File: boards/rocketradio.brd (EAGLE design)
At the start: 229.5 x 167.6 mm, 6 parts, among them X1 BU-SMA-H

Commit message: moving to new repo
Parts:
- added U$2: ATTINY85SOCKET, evan:SOCKET-08
- added U$3, U$4, U$5, U$6, U$7, U$8, U$9: 1N4148W, evan:SOD123
- U$1: value (none) -> DRA818V
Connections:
- new net N$10: U$1.3
- new net N$11: U$1.16, U$6.A
- new net N$12: U$8.C, U$9.A
- new net N$13: U$7.C, U$8.A
- new net N$14: U$2.5, U$7.A
- new net N$15: U$6.C
- new net N$16: U$3.A
- new net N$6: U$1.17, U$4.C
- new net N$7: U$4.A, U$5.C
- new net N$8: U$3.C, U$5.A
- new net N$9: U$1.18
- net +3V3: now also R2.1
- net GND: no longer R2.1
- net N$4: now also U$9.C
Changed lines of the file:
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@@
 <layer number="101" name="top_pads" color="7" fill="4" visible="no" active="yes"/>
 <layer number="102" name="bot_pads" color="7" fill="5" visible="no" active="yes"/>
+<layer number="103" name="tMap" color="7" fill="1" visible="yes" active="yes"/>
 <layer number="104" name="S_DOKU" color="7" fill="1" visible="no" active="yes"/>
+<layer number="105" name="tPlate" color="7" fill="1" visible="yes" active="yes"/>
+<layer number="106" name="bPlate" color="7" fill="1" visible="yes" active="yes"/>
+<layer number="107" name="Crop" color="7" fill="1" visible="yes" active="yes"/>
+<layer number="108" name="tplace-old" color="10" fill="1" visible="yes" active="yes"/>
+<layer number="109" name="ref-old" color="11" fill="1" visible="yes" active="yes"/>
 <layer number="116" name="Patch_BOT" color="9" fill="4" visible="yes" active="yes"/>
 <layer number="121" name="_tsilk" color="7" fill="1" visible="yes" active="yes"/>
 <layer number="122" name="_bsilk" color="7" fill="1" visible="yes" active="yes"/>
+<layer number="125" name="_tNames" color="7" fill="1" visible="yes" active="yes"/>
+<layer number="144" name="Drill_legend" color="7" fill="1" visible="yes" active="yes"/>
 <layer number="151" name="HeatSink" color="7" fill="1" visible="yes" active="yes"/>
 <layer number="199" name="Contour" color="7" fill="1" visible="no" active="yes"/>
@@
 <layer number="207" name="207bmp" color="8" fill="10" visible="yes" active="yes"/>
 <layer number="208" name="208bmp" color="9" fill="10" visible="yes" active="yes"/>
+<layer number="209" name="209bmp" color="7" fill="1" visible="yes" active="yes"/>
+<layer number="210" name="210bmp" color="7" fill="1" visible="yes" active="yes"/>
+<layer number="211" name="211bmp" color="7" fill="1" visible="yes" active="yes"/>
+<layer number="212" name="212bmp" color="7" fill="1" visible="yes" active="yes"/>
+<layer number="213" name="213bmp" color="7" fill="1" visible="yes" active="yes"/>
+<layer number="214" name="214bmp" color="7" fill="1" visible="yes" active="yes"/>
+<layer number="215" name="215bmp" color="7" fill="1" visible="yes" active="yes"/>
+<layer number="216" name="216bmp" color="7" fill="1" visible="yes" active="yes"/>
+<layer number="217" name="217bmp" color="18" fill="1" visible="no" active="no"/>
+<layer number="218" name="218bmp" color="19" fill="1" visible="no" active="no"/>
+<layer number="219" name="219bmp" color="20" fill="1" visible="no" active="no"/>
+<layer number="220" name="220bmp" color="21" fill="1" visible="no" active="no"/>
+<layer number="221" name="221bmp" color="22" fill="1" visible="no" active="no"/>
+<layer number="222" name="222bmp" color="23" fill="1" visible="no" active="no"/>
+<layer number="223" name="223bmp" color="24" fill="1" visible="no" active="no"/>
+<layer number="224" name="224bmp" color="25" fill="1" visible="no" active="no"/>
 <layer number="250" name="Descript" color="3" fill="1" visible="no" active="no"/>
 <layer number="251" name="SMDround" color="12" fill="11" visible="no" active="no"/>
@@
 </autorouter>
 <elements>
-<element name="U$1" library="dorji" package="DORJI" value="" x="1.27" y="-24.13"/>
+<element name="U$1" library="dorji" package="DORJI" value="DRA818V" x="1.27" y="-24.13"/>
 <element name="X1" library="con-coax" package="BU-SMA-H" value="BU-SMA-H" x="5.08" y="-35.56">
 <attribute name="OC_NEWARK" value="unknown" x="5.08" y="-35.56" size="1.778" layer="27" display="off"/>
@@
 <element name="R3" library="rcl" package="R0603" value="10K" x="2.54" y="-52.07"/>
 <element name="R4" library="rcl" package="R0603" value="10K" x="2.54" y="-55.88"/>
+<element name="U$2" library="evan" package="SOCKET-08" value="ATTINY85SOCKET" x="7.62" y="-64.77"/>
+<element name="U$3" library="evan" package="SOD123" value="1N4148W" x="3.81" y="-73.66"/>
+<element name="U$4" library="evan" package="SOD123" value="1N4148W" x="3.81" y="-80.01"/>
+<element name="U$5" library="evan" package="SOD123" value="1N4148W" x="3.81" y="-86.36"/>
+<element name="U$6" library="evan" package="SOD123" value="1N4148W" x="3.81" y="-92.71"/>
+<element name="U$7" library="evan" package="SOD123" value="1N4148W" x="3.81" y="-99.06"/>
+<element name="U$8" library="evan" package="SOD123" value="1N4148W" x="3.81" y="-105.41"/>
+<element name="U$9" library="evan" package="SOD123" value="1N4148W" x="3.81" y="-111.76"/>
 </elements>
 <signals>
@@
 <contactref element="R3" pad="1"/>
 <contactref element="R1" pad="1"/>
-<contactref element="R2" pad="1"/>
 <contactref element="R4" pad="1"/>
 <wire x1="1.69" y1="-52.07" x2="1.69" y2="-55.88" width="0" layer="19" extent="1-1"/>
-<wire x1="1.69" y1="-48.26" x2="1.69" y2="-52.07" width="0" layer="19" extent="1-1"/>
-<wire x1="1.69" y1="-44.45" x2="1.69" y2="-48.26" width="0" layer="19" extent="1-1"/>
+<wire x1="1.69" y1="-44.45" x2="1.69" y2="-52.07" width="0" layer="19" extent="1-1"/>
 <wire x1="2.5301" y1="-38.1099" x2="1.69" y2="-44.45" width="0" layer="19" extent="1-1"/>
 <wire x1="7.6299" y1="-38.1099" x2="2.5301" y2="-38.1099" width="0" layer="19" extent="1-1"/>
@@
 <signal name="+3V3">
 <contactref element="U$1" pad="8"/>
+<contactref element="R2" pad="1"/>
+<wire x1="38.27" y1="-7.73" x2="1.69" y2="-48.26" width="0" layer="19" extent="1-1"/>
 </signal>
 <signal name="N$1">
@@
 <contactref element="R3" pad="2"/>
 <contactref element="U$1" pad="5"/>
+<contactref element="U$9" pad="C"/>
+<wire x1="3.39" y1="-52.07" x2="1.91" y2="-111.76" width="0" layer="19" extent="1-1"/>
 <wire x1="23.47" y1="-3.63" x2="3.39" y2="-52.07" width="0" layer="19" extent="1-1"/>
 </signal>
@@
 <wire x1="5.47" y1="-3.63" x2="3.39" y2="-55.88" width="0" layer="19" extent="1-1"/>
 </signal>
+<signal name="N$6">
+<contactref element="U$1" pad="17"/>
+<contactref element="U$4" pad="C"/>
+<wire x1="10.17" y1="-25.53" x2="1.91" y2="-80.01" width="0" layer="19" extent="1-1"/>
+</signal>
+<signal name="N$7">
+<contactref element="U$4" pad="A"/>
+<contactref element="U$5" pad="C"/>
+<wire x1="5.71" y1="-80.01" x2="1.91" y2="-86.36" width="0" layer="19" extent="1-1"/>
+</signal>
+<signal name="N$8">
+<contactref element="U$5" pad="A"/>
+<contactref element="U$3" pad="C"/>
+<wire x1="1.91" y1="-73.66" x2="5.71" y2="-86.36" width="0" layer="19" extent="1-1"/>
+</signal>
+<signal name="N$11">
+<contactref element="U$6" pad="A"/>
+<contactref element="U$1" pad="16"/>
+<wire x1="14.57" y1="-25.53" x2="5.71" y2="-92.71" width="0" layer="19" extent="1-1"/>
+</signal>
+<signal name="N$12">
+<contactref element="U$9" pad="A"/>
+<contactref element="U$8" pad="C"/>
+<wire x1="1.91" y1="-105.41" x2="5.71" y2="-111.76" width="0" layer="19" extent="1-1"/>
+</signal>
+<signal name="N$13">
+<contactref element="U$8" pad="A"/>
+<contactref element="U$7" pad="C"/>
+<wire x1="1.91" y1="-99.06" x2="5.71" y2="-105.41" width="0" layer="19" extent="1-1"/>
+</signal>
+<signal name="N$9">
+<contactref element="U$1" pad="18"/>
+</signal>
+<signal name="N$10">
+<contactref element="U$1" pad="3"/>
+</signal>
+<signal name="N$14">
+<contactref element="U$7" pad="A"/>
+<contactref element="U$2" pad="5"/>
+<wire x1="11.43" y1="-60.96" x2="5.71" y2="-99.06" width="0" layer="19" extent="1-1"/>
+</signal>
+<signal name="N$15">
+<contactref element="U$6" pad="C"/>
+</signal>
+<signal name="N$16">
+<contactref element="U$3" pad="A"/>
+</signal>
 </signals>

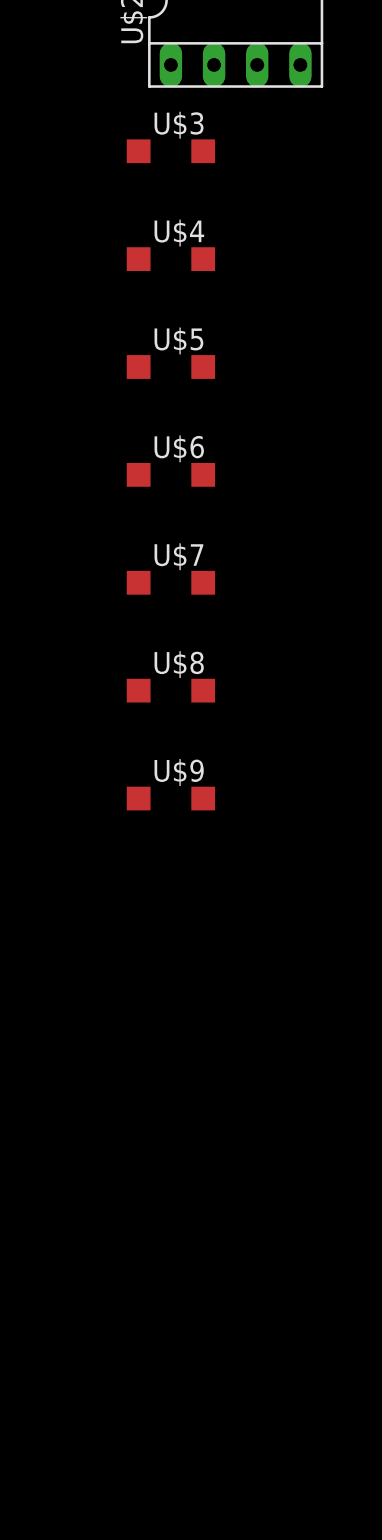
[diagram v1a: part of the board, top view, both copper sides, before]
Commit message: update board with correct modem pinout
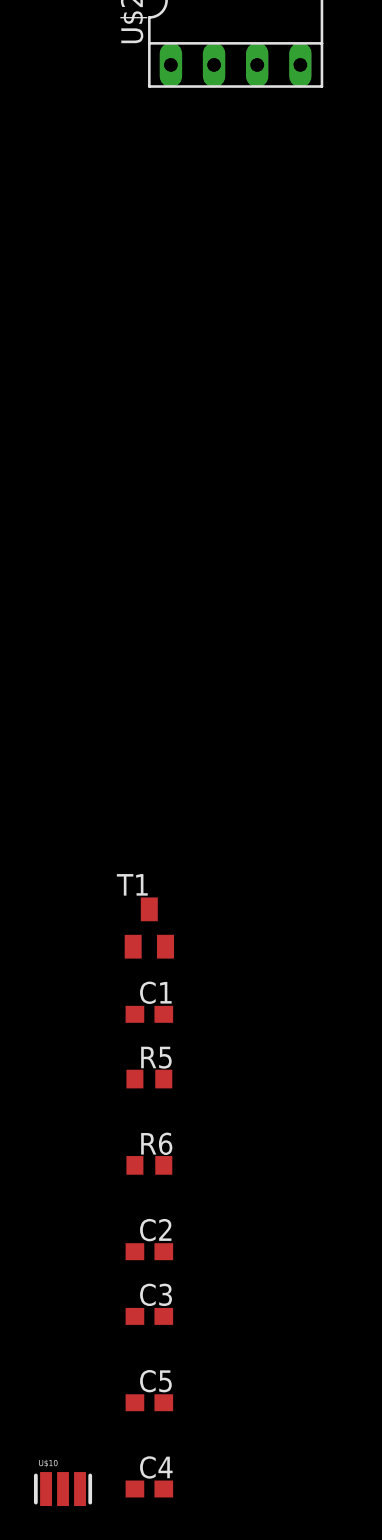
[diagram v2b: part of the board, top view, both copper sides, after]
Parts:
- removed U$3, U$4, U$5, U$6, U$7, U$8, U$9: 1N4148W, evan:SOD123
- added C1: (no value), rcl:C0603
- added C2, C4: 1uF, rcl:C0603
- added C3, C5: 0.1uF, rcl:C0603
- added R5: 30K, rcl:R0603
- added R6: 10K, rcl:R0603
- added T1: (no value), transistor:SOT23-BEC
- added U$10: CSTCE16M0V53-R0, evan:MYSMD2_RESONATOR
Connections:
- removed net N$10: U$1.3
- removed net N$11: U$1.16, U$6.A
- removed net N$12: U$8.C, U$9.A
- removed net N$13: U$7.C, U$8.A
- removed net N$14: U$2.5, U$7.A
- removed net N$4: R3.2, U$1.5, U$9.C
- removed net N$6: U$1.17, U$4.C
- removed net N$7: U$4.A, U$5.C
- removed net N$8: U$3.C, U$5.A
- new net MOD_IN: U$1.3, U$2.5
- new net MOD_OUT: U$2.6
- new net N$17: U$10.3, U$2.2
- new net N$18: U$10.1, U$2.3
- new net N$20: C1.1, R5.2, R6.1, T1.B
- new net SLAVE_SELECT: R3.2, U$1.5, U$2.1
- new net UART: U$2.7
- net +3V3: now also C2.1, C3.1, C4.1, C5.1, U$2.8
- net GND: now also C2.2, C3.2, C4.2, C5.2, U$10.2
- net N$15: now also U$1.16; no longer U$6.C
- net N$16: now also U$1.17; no longer U$3.A
- net N$9: now also C1.2
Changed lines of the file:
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@@
 <element name="R4" library="rcl" package="R0603" value="10K" x="2.54" y="-55.88"/>
 <element name="U$2" library="evan" package="SOCKET-08" value="ATTINY85SOCKET" x="7.62" y="-64.77"/>
-<element name="U$3" library="evan" package="SOD123" value="1N4148W" x="3.81" y="-73.66"/>
-<element name="U$4" library="evan" package="SOD123" value="1N4148W" x="3.81" y="-80.01"/>
-<element name="U$5" library="evan" package="SOD123" value="1N4148W" x="3.81" y="-86.36"/>
-<element name="U$6" library="evan" package="SOD123" value="1N4148W" x="3.81" y="-92.71"/>
-<element name="U$7" library="evan" package="SOD123" value="1N4148W" x="3.81" y="-99.06"/>
-<element name="U$8" library="evan" package="SOD123" value="1N4148W" x="3.81" y="-105.41"/>
-<element name="U$9" library="evan" package="SOD123" value="1N4148W" x="3.81" y="-111.76"/>
+<element name="T1" library="transistor" package="SOT23-BEC" value="" x="2.54" y="-119.38"/>
+<element name="C1" library="rcl" package="C0603" value="" x="2.54" y="-124.46"/>
+<element name="R5" library="rcl" package="R0603" value="30K" x="2.54" y="-128.27"/>
+<element name="R6" library="rcl" package="R0603" value="10K" x="2.54" y="-133.35"/>
+<element name="C2" library="rcl" package="C0603" value="1uF" x="2.54" y="-138.43"/>
+<element name="C3" library="rcl" package="C0603" value="0.1uF" x="2.54" y="-142.24"/>
+<element name="C4" library="rcl" package="C0603" value="1uF" x="2.54" y="-152.4"/>
+<element name="C5" library="rcl" package="C0603" value="0.1uF" x="2.54" y="-147.32"/>
+<element name="U$10" library="evan" package="MYSMD2_RESONATOR" value="CSTCE16M0V53-R0" x="-2.54" y="-152.4"/>
 </elements>
 <signals>
@@
 <contactref element="R1" pad="1"/>
 <contactref element="R4" pad="1"/>
+<contactref element="C3" pad="2"/>
+<contactref element="C2" pad="2"/>
+<contactref element="C5" pad="2"/>
+<contactref element="C4" pad="2"/>
+<contactref element="U$10" pad="2"/>
+<wire x1="3.39" y1="-152.4" x2="-2.54" y2="-152.4" width="0" layer="19" extent="1-1"/>
+<wire x1="3.39" y1="-147.32" x2="3.39" y2="-152.4" width="0" layer="19" extent="1-1"/>
+<wire x1="3.39" y1="-142.24" x2="3.39" y2="-147.32" width="0" layer="19" extent="1-1"/>
+<wire x1="3.39" y1="-138.43" x2="3.39" y2="-142.24" width="0" layer="19" extent="1-1"/>
+<wire x1="1.69" y1="-55.88" x2="3.39" y2="-138.43" width="0" layer="19" extent="1-1"/>
 <wire x1="1.69" y1="-52.07" x2="1.69" y2="-55.88" width="0" layer="19" extent="1-1"/>
 <wire x1="1.69" y1="-44.45" x2="1.69" y2="-52.07" width="0" layer="19" extent="1-1"/>
@@
 <contactref element="U$1" pad="8"/>
 <contactref element="R2" pad="1"/>
+<contactref element="C2" pad="1"/>
+<contactref element="C3" pad="1"/>
+<contactref element="C4" pad="1"/>
+<contactref element="C5" pad="1"/>
+<contactref element="U$2" pad="8"/>
+<wire x1="1.69" y1="-147.32" x2="1.69" y2="-152.4" width="0" layer="19" extent="1-1"/>
+<wire x1="1.69" y1="-142.24" x2="1.69" y2="-147.32" width="0" layer="19" extent="1-1"/>
+<wire x1="1.69" y1="-138.43" x2="1.69" y2="-142.24" width="0" layer="19" extent="1-1"/>
+<wire x1="3.81" y1="-60.96" x2="1.69" y2="-138.43" width="0" layer="19" extent="1-1"/>
+<wire x1="1.69" y1="-48.26" x2="3.81" y2="-60.96" width="0" layer="19" extent="1-1"/>
 <wire x1="38.27" y1="-7.73" x2="1.69" y2="-48.26" width="0" layer="19" extent="1-1"/>
-</signal>
-<signal name="N$1">
-<contactref element="U$1" pad="12"/>
-<contactref element="X1" pad="1"/>
-<wire x1="32.37" y1="-25.53" x2="5.08" y2="-35.56" width="0" layer="19" extent="1-1"/>
 </signal>
 <signal name="N$2">
@@
 <contactref element="U$1" pad="7"/>
 <wire x1="32.37" y1="-3.63" x2="3.39" y2="-44.45" width="0" layer="19" extent="1-1"/>
-</signal>
-<signal name="N$4">
-<contactref element="R3" pad="2"/>
-<contactref element="U$1" pad="5"/>
-<contactref element="U$9" pad="C"/>
-<wire x1="3.39" y1="-52.07" x2="1.91" y2="-111.76" width="0" layer="19" extent="1-1"/>
-<wire x1="23.47" y1="-3.63" x2="3.39" y2="-52.07" width="0" layer="19" extent="1-1"/>
 </signal>
 <signal name="N$3">
@@
 <wire x1="5.47" y1="-3.63" x2="3.39" y2="-55.88" width="0" layer="19" extent="1-1"/>
 </signal>
-<signal name="N$6">
-<contactref element="U$1" pad="17"/>
-<contactref element="U$4" pad="C"/>
-<wire x1="10.17" y1="-25.53" x2="1.91" y2="-80.01" width="0" layer="19" extent="1-1"/>
+<signal name="MOD_OUT">
+<contactref element="U$2" pad="6"/>
 </signal>
-<signal name="N$7">
-<contactref element="U$4" pad="A"/>
-<contactref element="U$5" pad="C"/>
-<wire x1="5.71" y1="-80.01" x2="1.91" y2="-86.36" width="0" layer="19" extent="1-1"/>
+<signal name="MOD_IN">
+<contactref element="U$1" pad="3"/>
+<contactref element="U$2" pad="5"/>
+<wire x1="14.57" y1="-3.63" x2="11.43" y2="-60.96" width="0" layer="19" extent="1-1"/>
 </signal>
-<signal name="N$8">
-<contactref element="U$5" pad="A"/>
-<contactref element="U$3" pad="C"/>
-<wire x1="1.91" y1="-73.66" x2="5.71" y2="-86.36" width="0" layer="19" extent="1-1"/>
+<signal name="UART">
+<contactref element="U$2" pad="7"/>
 </signal>
-<signal name="N$11">
-<contactref element="U$6" pad="A"/>
-<contactref element="U$1" pad="16"/>
-<wire x1="14.57" y1="-25.53" x2="5.71" y2="-92.71" width="0" layer="19" extent="1-1"/>
+<signal name="N$17">
+<contactref element="U$2" pad="2"/>
+<contactref element="U$10" pad="3"/>
+<wire x1="6.35" y1="-68.58" x2="-1.54" y2="-152.4" width="0" layer="19" extent="1-1"/>
 </signal>
-<signal name="N$12">
-<contactref element="U$9" pad="A"/>
-<contactref element="U$8" pad="C"/>
-<wire x1="1.91" y1="-105.41" x2="5.71" y2="-111.76" width="0" layer="19" extent="1-1"/>
+<signal name="N$18">
+<contactref element="U$2" pad="3"/>
+<contactref element="U$10" pad="1"/>
+<wire x1="8.89" y1="-68.58" x2="-3.54" y2="-152.4" width="0" layer="19" extent="1-1"/>
 </signal>
-<signal name="N$13">
-<contactref element="U$8" pad="A"/>
-<contactref element="U$7" pad="C"/>
-<wire x1="1.91" y1="-99.06" x2="5.71" y2="-105.41" width="0" layer="19" extent="1-1"/>
+<signal name="SLAVE_SELECT">
+<contactref element="U$2" pad="1"/>
+<contactref element="R3" pad="2"/>
+<contactref element="U$1" pad="5"/>
+<wire x1="3.39" y1="-52.07" x2="3.81" y2="-68.58" width="0" layer="19" extent="1-1"/>
+<wire x1="23.47" y1="-3.63" x2="3.39" y2="-52.07" width="0" layer="19" extent="1-1"/>
+</signal>
+<signal name="N$20">
+<contactref element="C1" pad="1"/>
+<contactref element="T1" pad="B"/>
+<contactref element="R5" pad="2"/>
+<contactref element="R6" pad="1"/>
+<wire x1="3.39" y1="-128.27" x2="1.69" y2="-133.35" width="0" layer="19" extent="1-1"/>
+<wire x1="1.69" y1="-124.46" x2="3.39" y2="-128.27" width="0" layer="19" extent="1-1"/>
+<wire x1="1.59" y1="-120.48" x2="1.69" y2="-124.46" width="0" layer="19" extent="1-1"/>
+</signal>
+<signal name="N$1">
+<contactref element="U$1" pad="12"/>
+<contactref element="X1" pad="1"/>
+<wire x1="32.37" y1="-25.53" x2="5.08" y2="-35.56" width="0" layer="19" extent="1-1"/>
 </signal>
 <signal name="N$9">
 <contactref element="U$1" pad="18"/>
-</signal>
-<signal name="N$10">
-<contactref element="U$1" pad="3"/>
-</signal>
-<signal name="N$14">
-<contactref element="U$7" pad="A"/>
-<contactref element="U$2" pad="5"/>
-<wire x1="11.43" y1="-60.96" x2="5.71" y2="-99.06" width="0" layer="19" extent="1-1"/>
+<contactref element="C1" pad="2"/>
+<wire x1="5.47" y1="-25.53" x2="3.39" y2="-124.46" width="0" layer="19" extent="1-1"/>
 </signal>
 <signal name="N$15">
-<contactref element="U$6" pad="C"/>
+<contactref element="U$1" pad="16"/>
 </signal>
 <signal name="N$16">
-<contactref element="U$3" pad="A"/>
+<contactref element="U$1" pad="17"/>
 </signal>
 </signals>

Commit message: add micro
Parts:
- added C10, C7, C8, C9: 0.1uF, rcl:C0603
- added C6: 1uF, rcl:C0603
- added R10, R11, R12, R7, R8, R9: (no value), rcl:R0603
- added U$3: ATTINY85SOCKET, evan:SOCKET-08
- C1: value (none) -> 0.1uF
- R5: value 30K -> (none)
- R6: value 10K -> (none)
- T1: value (none) -> 2N2222; device transistor:SOT23-BEC -> transistor:TO18
- moved U$2 120.8 mm to (12.7, 55.9)
- moved R4 109.0 mm to (41.9, 45.7), turned to 270 degrees
- moved R3 106.9 mm to (45.7, 45.7), turned to 270 degrees
- moved R2 105.1 mm to (49.5, 45.7), turned to 270 degrees
- moved R1 103.5 mm to (53.3, 45.7), turned to 270 degrees
- moved C1 66.2 mm to (-2.54, -190.5)
- moved X1 63.1 mm to (53.3, 5.08), turned to 270 degrees
- moved T1 54.7 mm to (0.00, -174.0)
- moved R5 52.3 mm to (-2.54, -180.3)
- moved R6 52.3 mm to (-2.54, -185.4)
- moved U$1 44.9 mm to (22.9, 15.2)
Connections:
- removed net N$15: U$1.16
- removed net N$16: U$1.17
- removed net N$20: C1.1, R5.2, R6.1, T1.B
- removed net N$9: C1.2, U$1.18
- new net MIC_IN: C8.1, U$1.18
- new net N$10: C9.1, R9.2, T1.1
- new net N$11: C10.1, R10.1, T1.3
- new net N$6: C8.2, R7.2, R8.1
- new net N$7: C1.1, R5.1, R6.2, T1.2
- new net N$8: C1.2, U$1.3
- new net RADIO_CONTROL: U$1.16, U$3.2
- net +3V3: now also C6.1, C7.1, R1.1, R10.2, R11.2, R3.1, R5.2, U$3.8
- net GND: now also C6.2, C7.2, C9.2, R12.1, R6.1, R8.2, R9.1, U$2.4, U$3.4; no longer R1.1, R3.1
- net MOD_IN: now also C10.2, R11.1, R12.2; no longer U$1.3
- net MOD_OUT: now also R7.1
- net SLAVE_SELECT: now also U$3.1
- net UART: now also U$3.7
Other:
- board size 229.5 x 167.6 mm -> 103.8 x 82.5 mm
